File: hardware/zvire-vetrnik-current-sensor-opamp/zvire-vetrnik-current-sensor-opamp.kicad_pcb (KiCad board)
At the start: 2 copper layers, 58.4 x 24.1 mm, 25 parts, among them J1 Conn_01x03, J2 Conn_Coaxial, J3 Conn_01x03, SW1 DP-06, U1 LMV358

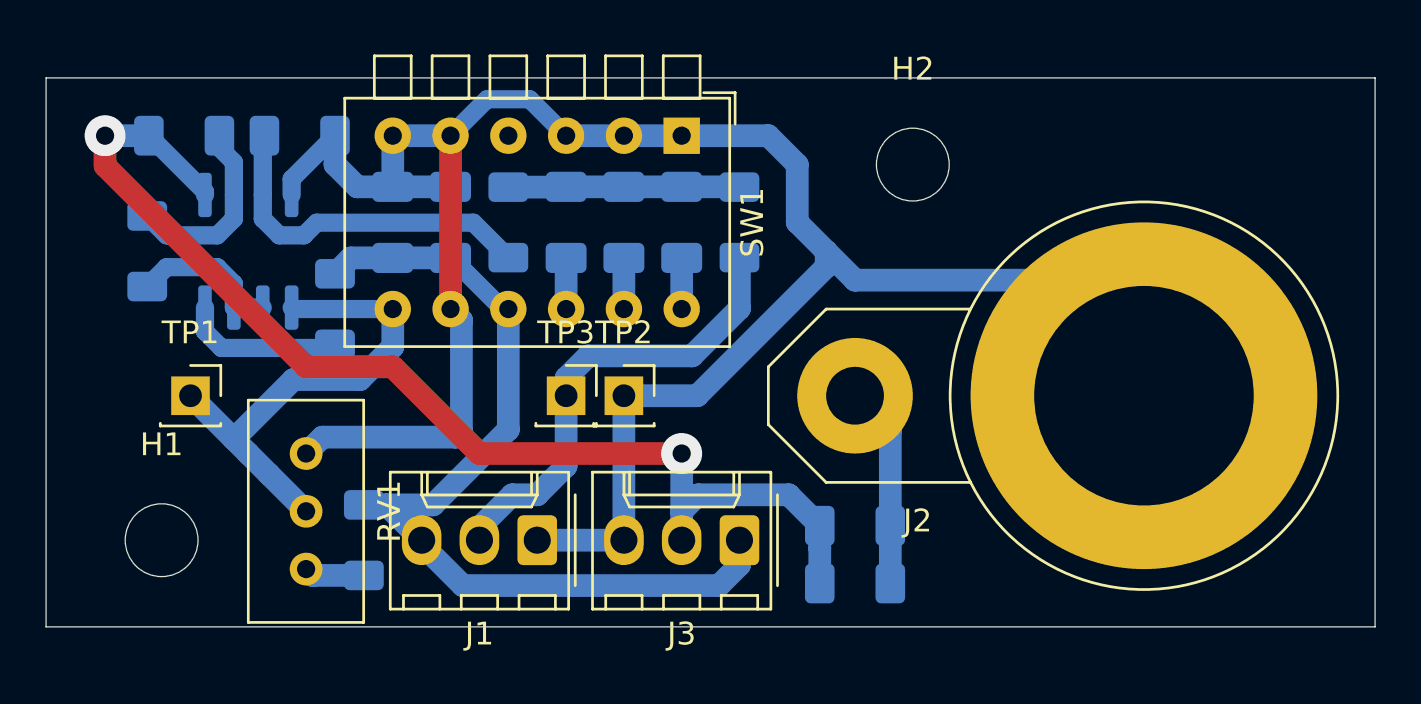
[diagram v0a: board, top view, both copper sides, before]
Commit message: [hardware] Resistor values in current-sensor-opamp
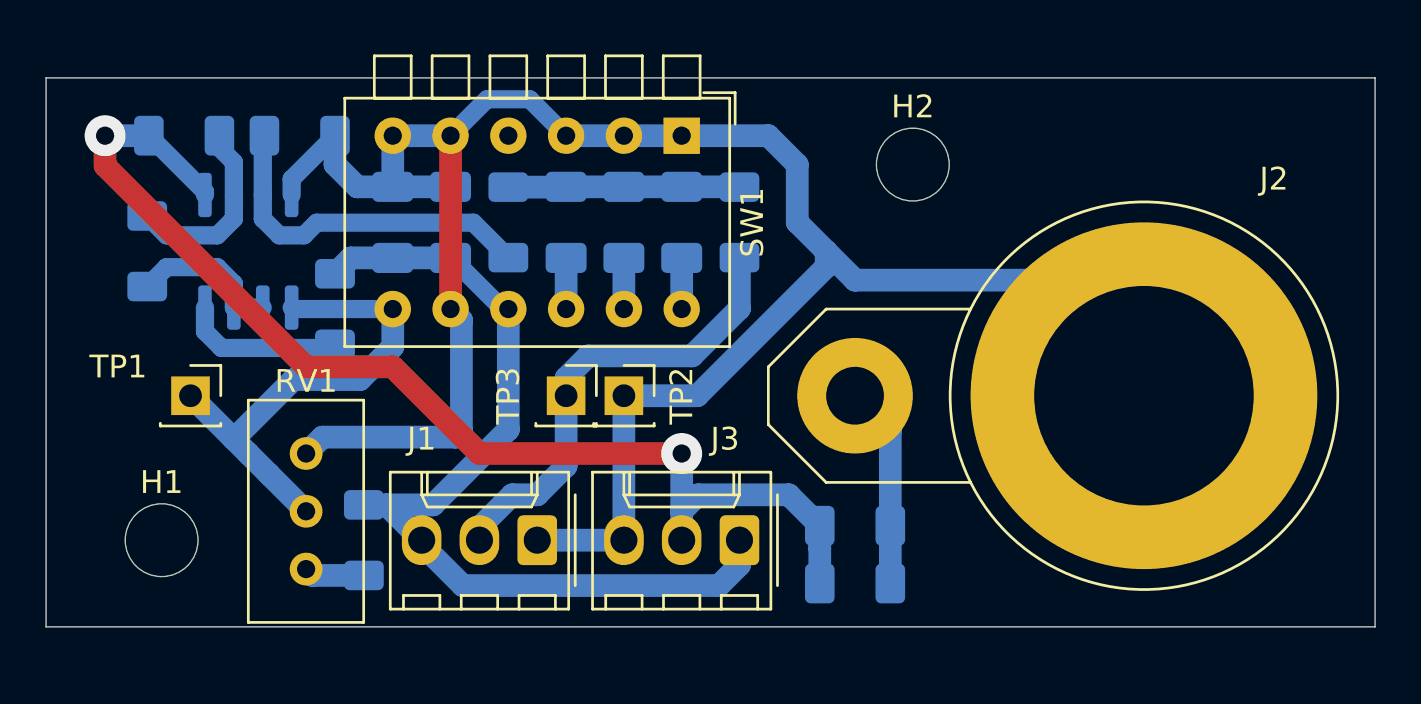
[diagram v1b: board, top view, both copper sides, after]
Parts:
- R6, R7: value 120k -> 150k

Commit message: Add current-sensor-opamp notes
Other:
- board text added: "WARNING: BNC shield is GNDPWR"
